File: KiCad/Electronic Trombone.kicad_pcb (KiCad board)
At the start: 2 copper layers, 150 x 100 mm, 174 parts, among them J1 691137710002, J2 691137710003, J3 691137710003, J4 691137710002, J5 691137710002, Q1 NPN, Q2 PNP, Q3 NPN, Q4 PNP, Q5 NPN, Q6 NPN, SW1 SW_Push_Dual, SW2 SW_Push_Dual, SW3 SW_Push_Dual, SW4 SW_DPST, U1 CD74HC4051E, U10 TL074, U11 TL074, U2 TL074, U3 TL074, U4 40106, U5 TL074, U6 TL074, U7 TL074, U8 TL074, U9 TL074

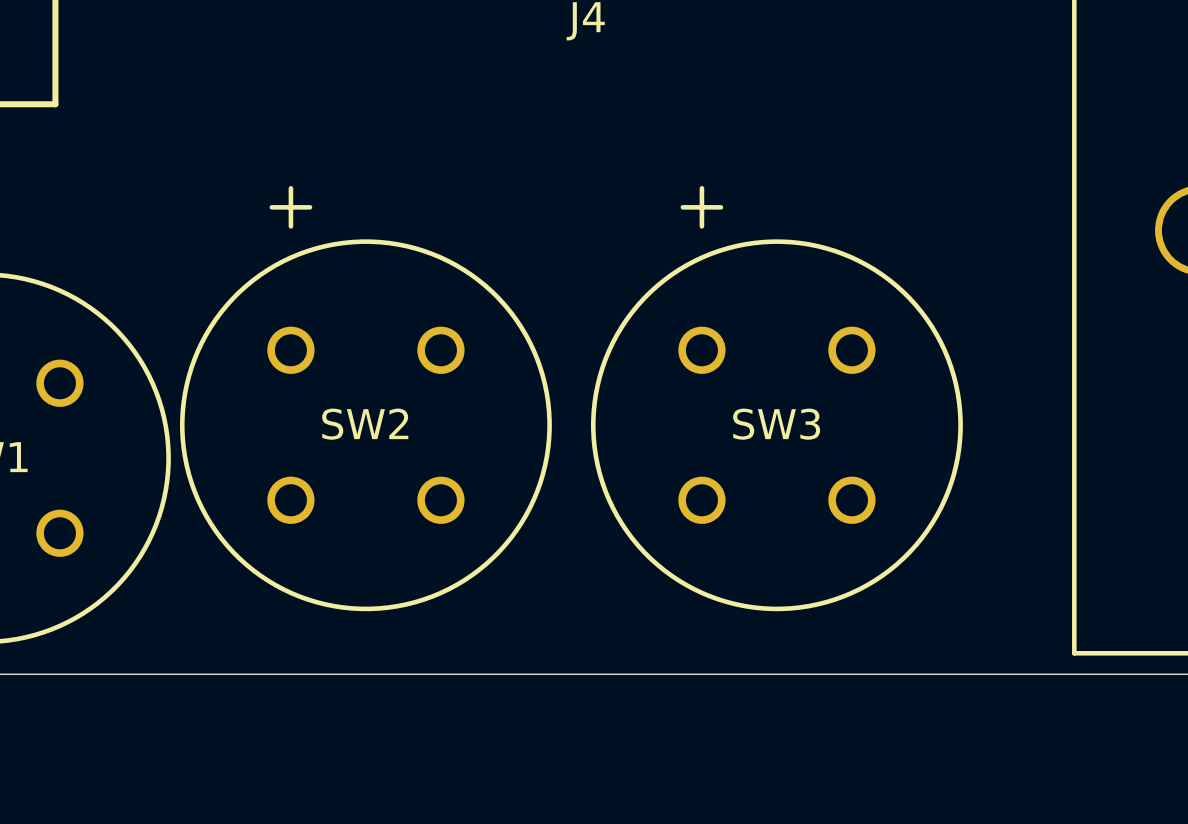
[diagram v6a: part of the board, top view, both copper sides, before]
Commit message: corrected push button's symbol on schematic
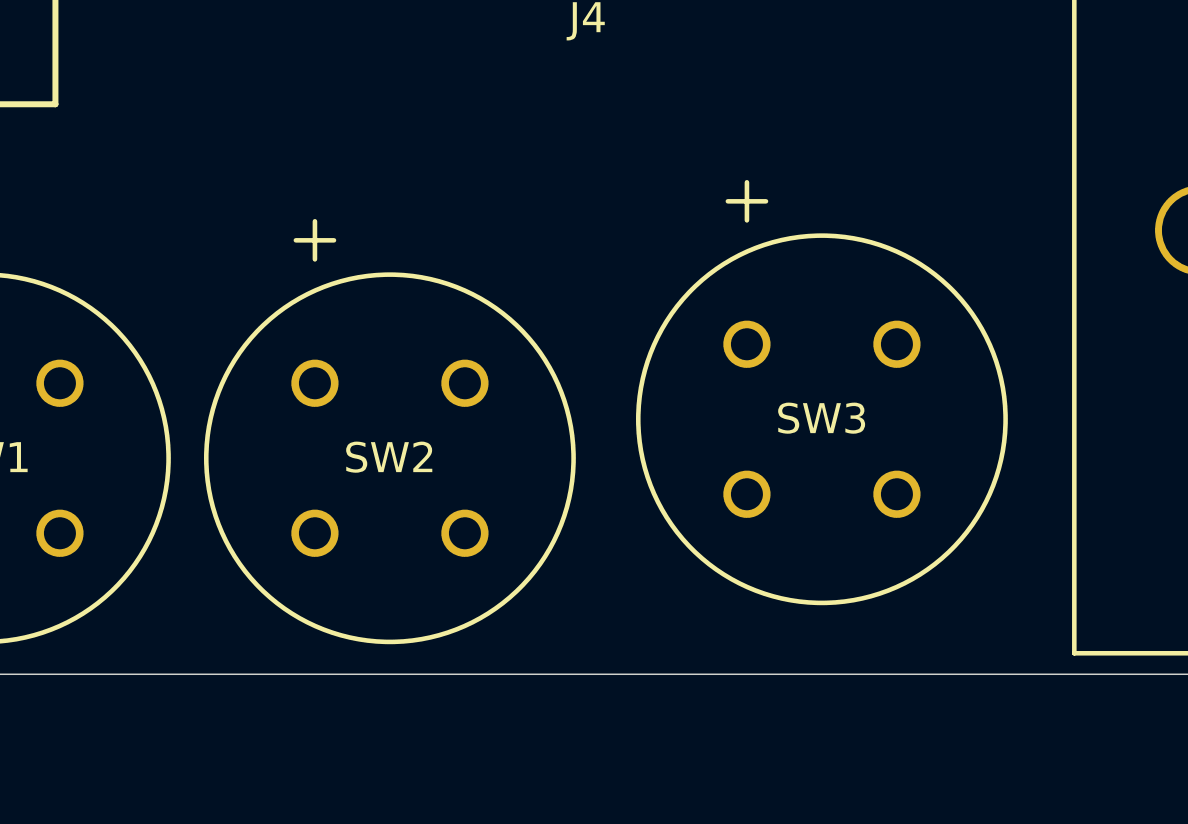
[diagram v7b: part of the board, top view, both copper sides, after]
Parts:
- SW1, SW2, SW3: value SW_Push_Dual -> D6R90F2LFS
- moved SW3 1.51 mm to (82.4, 139.0)
- moved SW2 1.36 mm to (68.0, 140.3)
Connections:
- SW1 pad 3: +5V -> Net-(J3-Pad1)
- SW1 pad 4: Net-(J3-Pad1) -> +5V
- SW2 pad 3: +5V -> Net-(J3-Pad2)
- SW2 pad 4: Net-(J3-Pad2) -> +5V
- SW3 pad 3: +5V -> Net-(J3-Pad3)
- SW3 pad 4: Net-(J3-Pad3) -> +5V
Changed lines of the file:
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@@
 	(footprint "Switch Push Button D6R90F2LFS:D6R90_CNK"
 		(layer "F.Cu")
-		(at 67.2 139.2)
+		(at 68 140.3)
 		(tags "D6R90F2LFS ")
 		(property "Reference" "SW2"
@@
 			)
 		)
-		(property "Value" "SW_Push_Dual"
+		(property "Value" "D6R90F2LFS"
 			(at 2.5 2.499995 0)
 			(unlocked yes)
@@
 			)
 		)
-		(property "Datasheet" ""
+		(property "Datasheet" "D6R90F2LFS"
 			(at 0 0 0)
 			(layer "F.Fab")
@@
 			)
 		)
-		(property "Description" "Push button switch, generic, symbol, four pins"
+		(property "Description" ""
 			(at 0 0 0)
 			(layer "F.Fab")
@@
 			)
 		)
+		(property ki_fp_filters "D6R90_CNK")
 		(sheetname "/Button Controls/")
 		(sheetfile "Button Controls.kicad_sch")
@@
 			(unit
 				(name "A")
-				(pins "1" "3" "2" "4")
+				(pins "1" "2" "4" "3")
 			)
 		)
@@
 			(net "+5V")
 			(pinfunction "1_1")
-			(pintype "passive")
+			(pintype "unspecified")
 		)
 		(pad "2" thru_hole circle
@@
 			(net "Net-(J3-Pad2)")
 			(pinfunction "2_2")
-			(pintype "passive")
+			(pintype "unspecified")
 		)
 		(pad "3" thru_hole circle
@@
 			(layers "*.Cu" "*.Mask")
 			(remove_unused_layers no)
-			(net "+5V")
+			(net "Net-(J3-Pad2)")
 			(pinfunction "3_3")
-			(pintype "passive")
+			(pintype "unspecified")
 		)
 		(pad "4" thru_hole circle
@@
 			(layers "*.Cu" "*.Mask")
 			(remove_unused_layers no)
-			(net "Net-(J3-Pad2)")
+			(net "+5V")
 			(pinfunction "4_4")
-			(pintype "passive")
+			(pintype "unspecified")
 		)
 		(embedded_fonts no)
@@
 			)
 		)
-		(property "Value" "SW_Push_Dual"
+		(property "Value" "D6R90F2LFS"
 			(at 2.5 2.499995 0)
 			(unlocked yes)
@@
 			)
 		)
-		(property "Datasheet" ""
+		(property "Datasheet" "D6R90F2LFS"
 			(at 0 0 0)
 			(layer "F.Fab")
@@
 			)
 		)
-		(property "Description" "Push button switch, generic, symbol, four pins"
+		(property "Description" ""
 			(at 0 0 0)
 			(layer "F.Fab")
@@
 			)
 		)
+		(property ki_fp_filters "D6R90_CNK")
 		(sheetname "/Button Controls/")
 		(sheetfile "Button Controls.kicad_sch")
@@
 			(unit
 				(name "A")
-				(pins "1" "3" "2" "4")
+				(pins "1" "2" "4" "3")
 			)
 		)
@@
 			(net "+5V")
 			(pinfunction "1_1")
-			(pintype "passive")
+			(pintype "unspecified")
 		)
 		(pad "2" thru_hole circle
@@
 			(net "Net-(J3-Pad1)")
 			(pinfunction "2_2")
-			(pintype "passive")
+			(pintype "unspecified")
 		)
 		(pad "3" thru_hole circle
@@
 			(layers "*.Cu" "*.Mask")
 			(remove_unused_layers no)
-			(net "+5V")
+			(net "Net-(J3-Pad1)")
 			(pinfunction "3_3")
-			(pintype "passive")
+			(pintype "unspecified")
 		)
 		(pad "4" thru_hole circle
@@
 			(layers "*.Cu" "*.Mask")
 			(remove_unused_layers no)
-			(net "Net-(J3-Pad1)")
+			(net "+5V")
 			(pinfunction "4_4")
-			(pintype "passive")
+			(pintype "unspecified")
 		)
 		(embedded_fonts no)
@@
 	(footprint "Switch Push Button D6R90F2LFS:D6R90_CNK"
 		(layer "F.Cu")
-		(at 80.9 139.2)
+		(at 82.4 139)
 		(tags "D6R90F2LFS ")
 		(property "Reference" "SW3"
@@
 			)
 		)
-		(property "Value" "SW_Push_Dual"
+		(property "Value" "D6R90F2LFS"
 			(at 2.5 2.499995 0)
 			(unlocked yes)
@@
 			)
 		)
-		(property "Datasheet" ""
+		(property "Datasheet" "D6R90F2LFS"
 			(at 0 0 0)
 			(layer "F.Fab")
@@
 			)
 		)
-		(property "Description" "Push button switch, generic, symbol, four pins"
+		(property "Description" ""
 			(at 0 0 0)
 			(layer "F.Fab")
@@
 			)
 		)
+		(property ki_fp_filters "D6R90_CNK")
 		(sheetname "/Button Controls/")
 		(sheetfile "Button Controls.kicad_sch")
@@
 			(unit
 				(name "A")
-				(pins "1" "3" "2" "4")
+				(pins "1" "2" "4" "3")
 			)
 		)
@@
 			(net "+5V")
 			(pinfunction "1_1")
-			(pintype "passive")
+			(pintype "unspecified")
 		)
 		(pad "2" thru_hole circle
@@
 			(net "Net-(J3-Pad3)")
 			(pinfunction "2_2")
-			(pintype "passive")
+			(pintype "unspecified")
 		)
 		(pad "3" thru_hole circle
@@
 			(layers "*.Cu" "*.Mask")
 			(remove_unused_layers no)
-			(net "+5V")
+			(net "Net-(J3-Pad3)")
 			(pinfunction "3_3")
-			(pintype "passive")
+			(pintype "unspecified")
 		)
 		(pad "4" thru_hole circle
@@
 			(layers "*.Cu" "*.Mask")
 			(remove_unused_layers no)
-			(net "Net-(J3-Pad3)")
+			(net "+5V")
 			(pinfunction "4_4")
-			(pintype "passive")
+			(pintype "unspecified")
 		)
 		(embedded_fonts no)
